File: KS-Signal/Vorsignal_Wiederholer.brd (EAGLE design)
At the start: 24.6 x 40.5 mm, 24 parts, among them IC1 ATTINY44SSU, Q1 IRLML5203, X1 SSW-106-02-S-S-RA, X2 TSW-106-02-S-S-RA

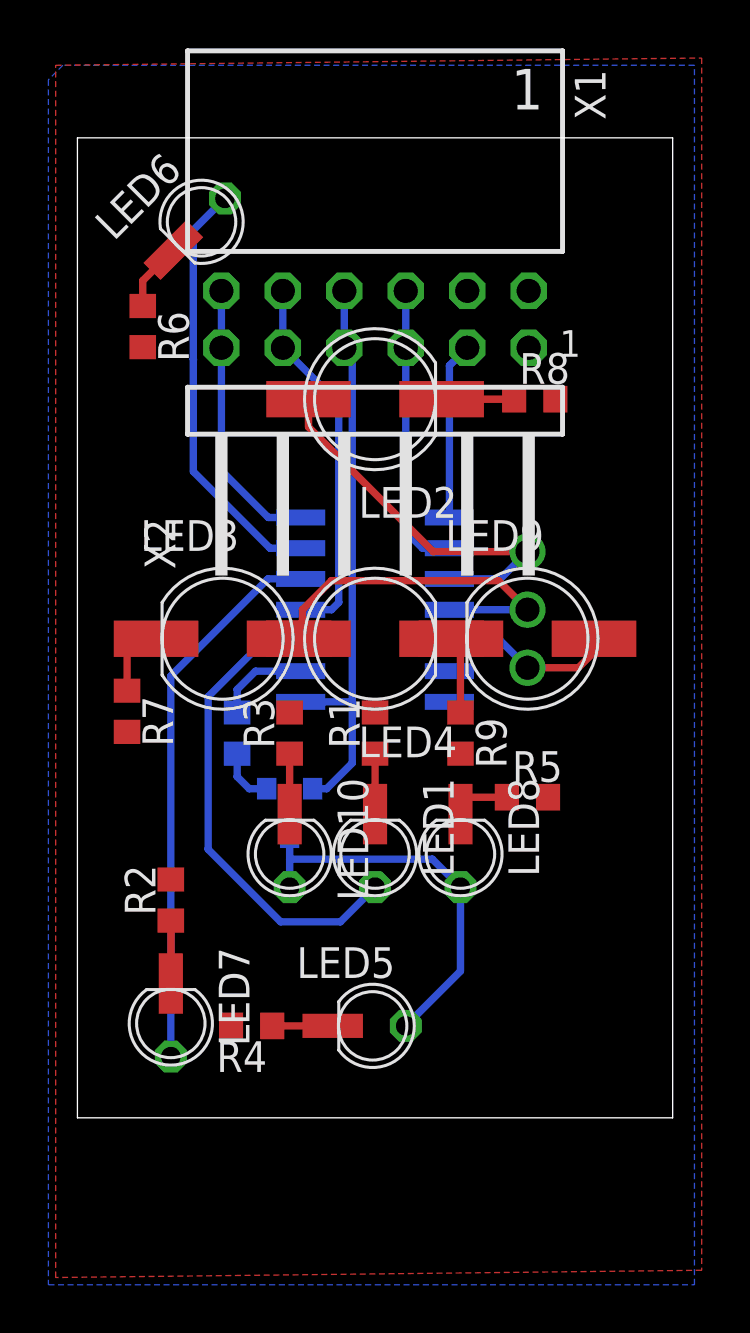
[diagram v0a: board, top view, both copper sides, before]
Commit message: Vorsignale fertiggestellt
- Vorsignalschirme fertiggestellt
- Platinengrößen angepasst
-> Achtung: Stecker und Pinbelegung unterschiedlich zwischen den beiden Vorsignaltypen
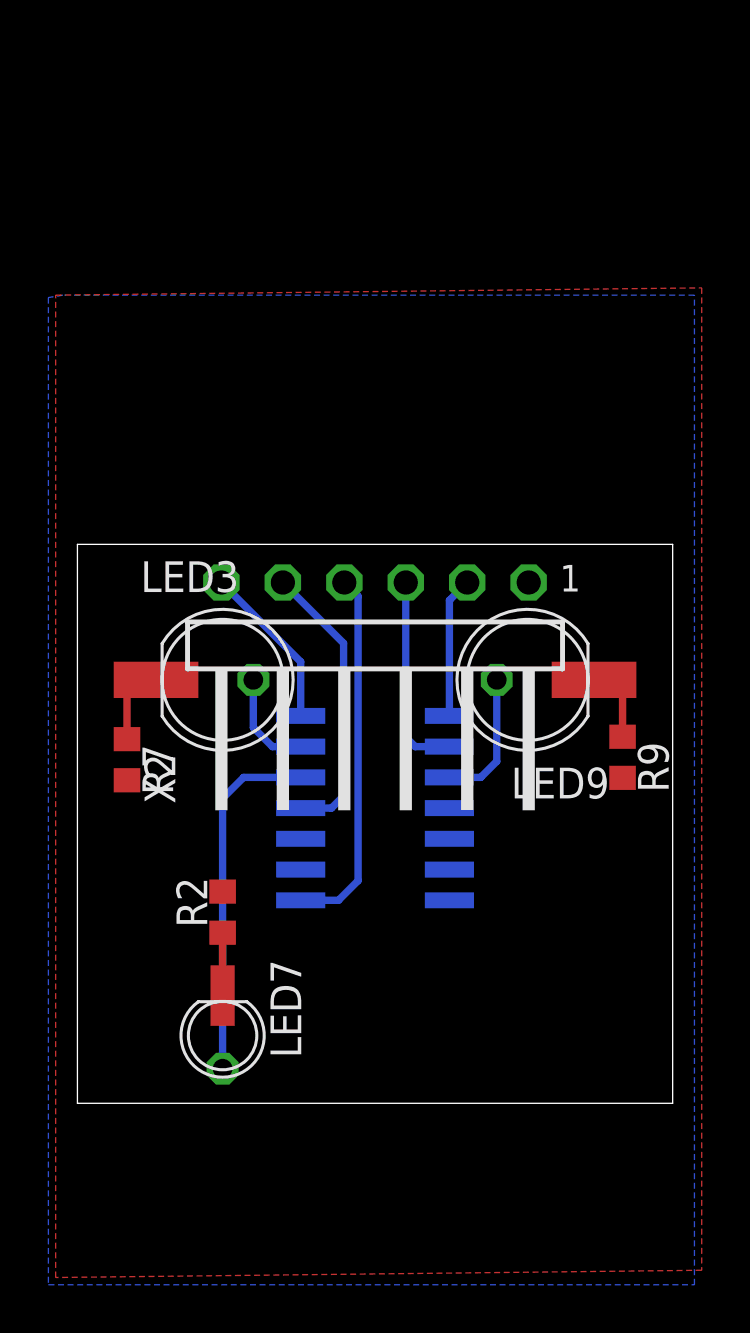
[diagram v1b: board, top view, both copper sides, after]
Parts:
- removed LED1, LED10, LED5, LED6, LED8: LED_SMD3MM_SMD/DIP, LEDFLATTOP:3MM_FLAT/DIP_SMDLED
- removed LED2, LED4: LED_SMD5MM_SMD, LEDFLATTOP:5MM_FLAT_SMDLED
- removed Q1: IRLML5203, transistor-power:MICRO3
- removed R1, R10, R3, R4, R5, R6, R8: (no value), rcl:R0603
- removed X1: SSW-106-02-S-S-RA, con-samtec:SSW-106-02-S-S-RA
- LED3, LED9: value LED_SMD5MM_SMD -> LED_SMD5MM_SMD/DIP; device LEDFLATTOP:5MM_FLAT_SMDLED -> LEDFLATTOP:5MM_FLAT/DIP_SMDLED
- moved X2 9.70 mm to (12.3, 26.3)
- moved IC1 8.20 mm to (12.3, 18.5)
- moved R9 6.77 mm to (22.5, 20.6)
- moved LED7 2.20 mm to (6.00, 9.00)
- moved R2 2.20 mm to (6.00, 14.2)
- moved R7 2.00 mm to (2.05, 20.5)
- moved LED3 1.70 mm to (6.00, 23.8)
- moved LED9 1.70 mm to (18.6, 23.8), turned to 180 degrees
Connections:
- net SH1 renamed WH
- removed net N$10: LED10.+, LED5.+, LED8.+, Q1.3
- removed net N$11: Q1.1, R10.2
- removed net N$2: LED6.-, R6.1
- removed net N$3: LED8.-, R5.1
- removed net N$4: LED5.-, R4.1
- removed net N$5: LED10.-, R3.1
- removed net N$7: LED1.-, R1.1
- removed net N$9: LED2.-, R8.1
- removed net NC: X1.2
- removed net RT: IC1.10, LED2.+
- removed net SH1ZS1: IC1.3, LED1.+
- removed net ZL: IC1.6, LED6.+
- removed net ZS7: IC1.2, R10.1
- net GE: now also IC1.10; no longer IC1.12
- net GN: now also IC1.6; no longer IC1.11, LED4.+
- net GND: no longer R1.2, R3.2, R4.2, R5.2, R6.2, R8.2, X1.1
- net N$1: no longer LED4.-
- net RESET: no longer X1.5
- net SCL/SCK: no longer X1.3
- net SDA/MOSI: no longer X1.6
- net VCC: no longer Q1.2, X1.4
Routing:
- net SH1ZS1: track 19.9 -> 0.00 mm
- net ZL: track 17.6 -> 0.00 mm
- net N$10: track 16.3 -> 0.00 mm
- net RT: track 16.1 -> 0.00 mm, vias 1 -> 0
- net GN: track 15.8 -> 4.25 mm, vias 1 -> 0
- net VCC: track 23.9 -> 15.3 mm
- net WH: track 22.8 -> 14.8 mm
- net SDA/MOSI: track 11.5 -> 6.87 mm
- net ZS7: track 3.89 -> 0.00 mm
- net RESET: track 15.5 -> 11.8 mm
- net SCL/SCK: track 12.0 -> 8.36 mm
- net N$9: track 3.00 -> 0.00 mm
- net N$2: track 2.84 -> 0.00 mm
- net N$3: track 2.62 -> 0.00 mm
- net N$7: track 2.50 -> 0.00 mm
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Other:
- board size 24.6 x 40.5 mm -> 24.6 x 23.1 mm
